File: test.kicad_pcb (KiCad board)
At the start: 2 copper layers, 112 x 43 mm, 41 parts, among them IC1 QFN50P300X300X100-17N-D, IC2 SOT95P280X145-6N, IC3 ESP32-S3-WROOM-1-N16, J1 UART0, J2 73100-0105, J3 73100-0105, K1 AQY210EHA, SW1 Reset, SW2 Boot, U1 USB-C_SMD-TYPE-C-31-M-12, U2 1043, U3 1043, U4 LD1086DT33TR, U5 LD1086DT33TR

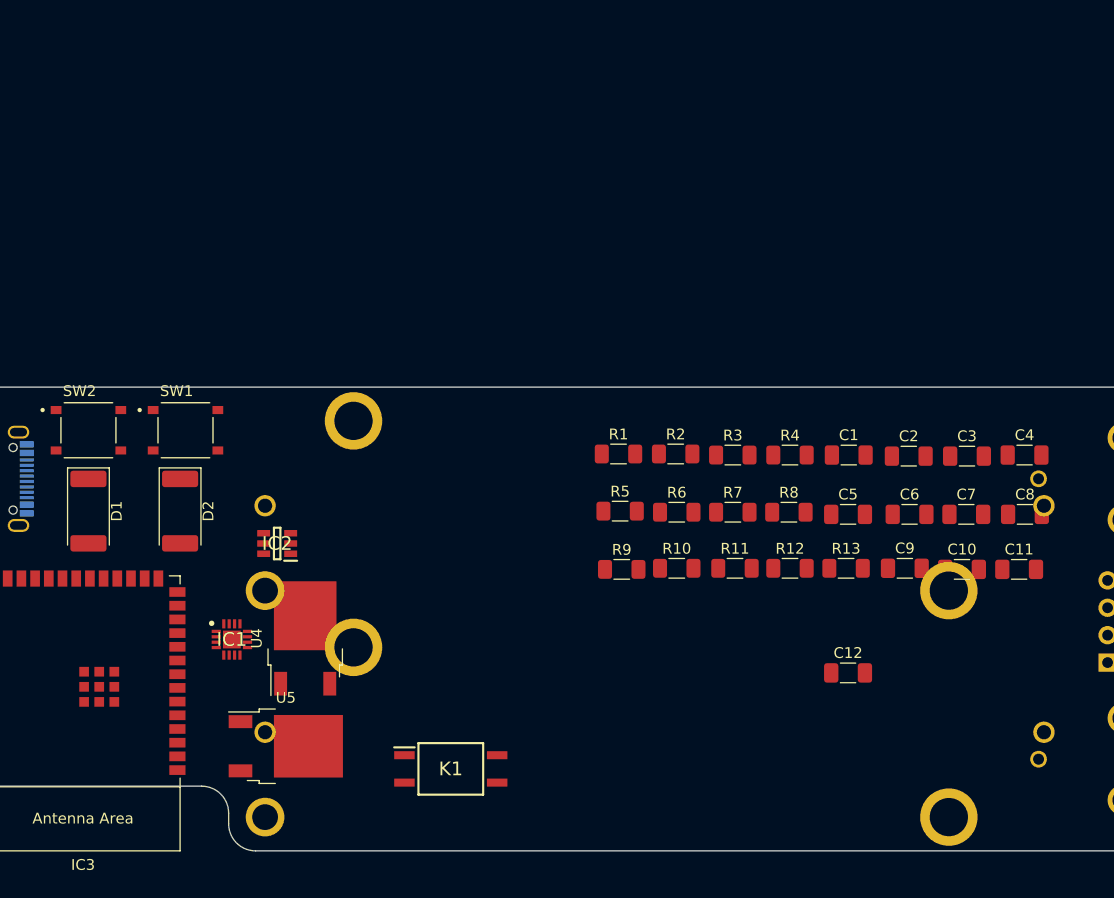
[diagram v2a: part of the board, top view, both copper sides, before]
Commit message: added dac and changed switch, gain
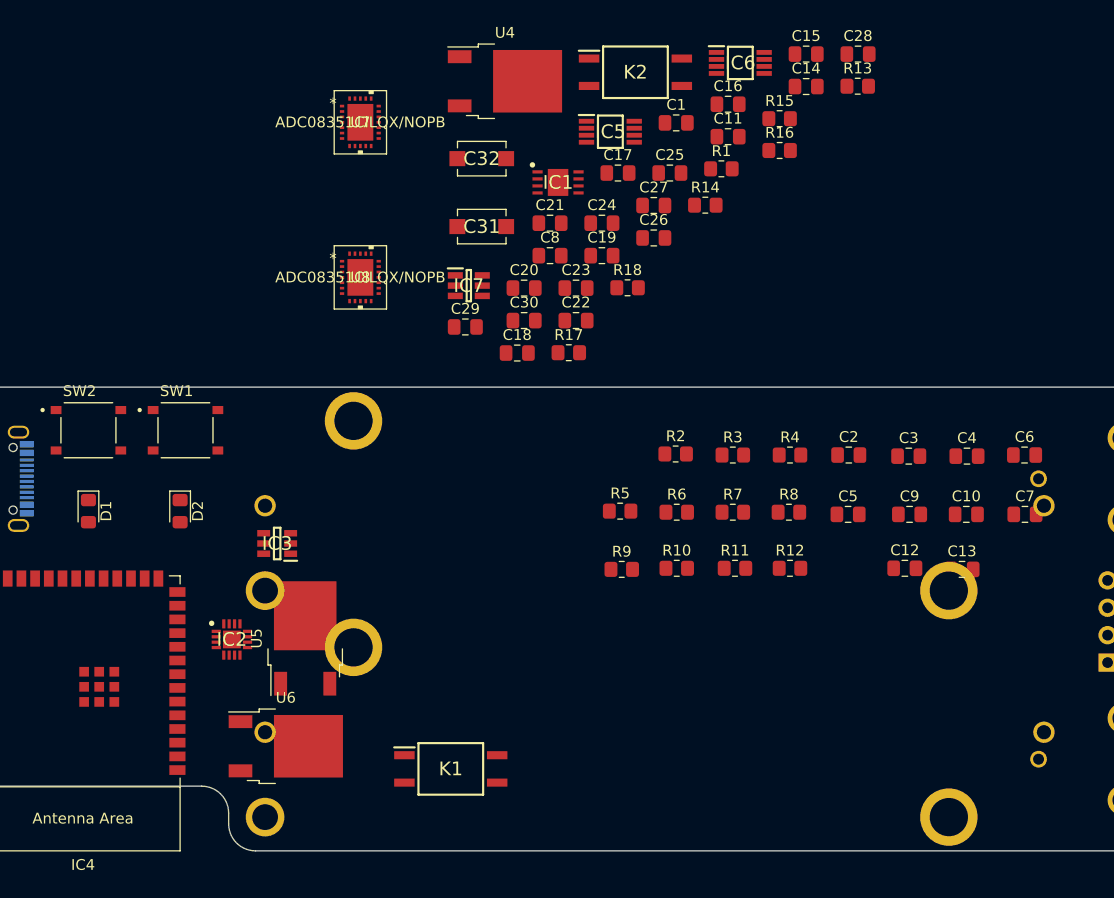
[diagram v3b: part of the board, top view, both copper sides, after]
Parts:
- removed the C12 at (110.9, 116.5)
- added C1: 1u, Capacitor_SMD:C_0805_2012Metric_Pad1.18x1.45mm_HandSolder, F.Cu at (95.0, 65.5)
- added C14: 0.1u, Capacitor_SMD:C_0805_2012Metric_Pad1.18x1.45mm_HandSolder, F.Cu at (107.0, 62.1)
- added C15: 0.1u, Capacitor_SMD:C_0805_2012Metric_Pad1.18x1.45mm_HandSolder, F.Cu at (107.0, 59.1)
- added C16: 0.1u, Capacitor_SMD:C_0805_2012Metric_Pad1.18x1.45mm_HandSolder, F.Cu at (99.8, 63.8)
- added C17: 10u, Capacitor_SMD:C_0805_2012Metric_Pad1.18x1.45mm_HandSolder, F.Cu at (89.6, 70.2)
- added C18: 10u, Capacitor_SMD:C_0805_2012Metric_Pad1.18x1.45mm_HandSolder, F.Cu at (80.3, 86.8)
- added C19: 10u, Capacitor_SMD:C_0805_2012Metric_Pad1.18x1.45mm_HandSolder, F.Cu at (88.1, 77.8)
- added C20: 0.1u, Capacitor_SMD:C_0805_2012Metric_Pad1.18x1.45mm_HandSolder, F.Cu at (80.9, 80.8)
- added C21: 0.1u, Capacitor_SMD:C_0805_2012Metric_Pad1.18x1.45mm_HandSolder, F.Cu at (83.3, 74.8)
- added C22: 0.1u, Capacitor_SMD:C_0805_2012Metric_Pad1.18x1.45mm_HandSolder, F.Cu at (85.7, 83.8)
- added C23: 0.1u, Capacitor_SMD:C_0805_2012Metric_Pad1.18x1.45mm_HandSolder, F.Cu at (85.7, 80.8)
- added C24: 10u, Capacitor_SMD:C_0805_2012Metric_Pad1.18x1.45mm_HandSolder, F.Cu at (88.1, 74.8)
- added C25: 10u, Capacitor_SMD:C_0805_2012Metric_Pad1.18x1.45mm_HandSolder, F.Cu at (94.4, 70.2)
- added C26: 0.1u, Capacitor_SMD:C_0805_2012Metric_Pad1.18x1.45mm_HandSolder, F.Cu at (92.9, 76.2)
- added C27: 47n, Capacitor_SMD:C_0805_2012Metric_Pad1.18x1.45mm_HandSolder, F.Cu at (92.9, 73.2)
- added C28: 47n, Capacitor_SMD:C_0805_2012Metric_Pad1.18x1.45mm_HandSolder, F.Cu at (111.9, 59.1)
- added C29: 100n, Capacitor_SMD:C_0805_2012Metric_Pad1.18x1.45mm_HandSolder, F.Cu at (75.5, 84.4)
- added C30: 100n, Capacitor_SMD:C_0805_2012Metric_Pad1.18x1.45mm_HandSolder, F.Cu at (80.9, 83.8)
- added C31: 5.5p-30p var, project_library:JZ300, F.Cu at (77.0, 75.1)
- added C32: 5.5p-30p var, project_library:JZ300, F.Cu at (77.0, 68.8)
- added C8: 10u, Capacitor_SMD:C_0805_2012Metric_Pad1.18x1.45mm_HandSolder, F.Cu at (83.3, 77.8)
- added IC1: LC709203FQH-01TWG, project_library:LC709203FQH-01TWG, F.Cu at (84.0, 71.0)
- added IC5: MCP6S91-E_MS, project_library:MCP6S91-E_MS, F.Cu at (88.9, 66.3)
- added IC6: MCP6S91-E_MS, project_library:MCP6S91-E_MS, F.Cu at (100.9, 59.9)
- added IC7: MCP4726A1T-E_CH, project_library:MCP4726A1T-E_CH, F.Cu at (75.8, 80.6)
- added K2: AQY210EHA, project_library:AQY210EHAX, F.Cu at (91.2, 60.8)
- added R14: 1k, Resistor_SMD:R_0805_2012Metric_Pad1.20x1.40mm_HandSolder, F.Cu at (97.7, 73.1)
- added R15: 100k, Resistor_SMD:R_0805_2012Metric_Pad1.20x1.40mm_HandSolder, F.Cu at (104.6, 65.1)
- added R16: 100k, Resistor_SMD:R_0805_2012Metric_Pad1.20x1.40mm_HandSolder, F.Cu at (104.6, 68.1)
- added R17: 910k, Resistor_SMD:R_0805_2012Metric_Pad1.20x1.40mm_HandSolder, F.Cu at (85.0, 86.8)
- added R18: 910k, Resistor_SMD:R_0805_2012Metric_Pad1.20x1.40mm_HandSolder, F.Cu at (90.5, 80.8)
- added U4: LD1086DT33TR, Package_TO_SOT_SMD:TO-252-2, F.Cu at (79.1, 61.6)
- added U7: ADC08351CILQX/NOPB, project_library:ADC08351CILQX, F.Cu at (65.7, 65.4)
- added U8: ADC08351CILQX/NOPB, project_library:ADC08351CILQX, F.Cu at (65.7, 79.8)
- C10: renamed from C7; footprint Capacitor_SMD:C_1206_3216Metric_Pad1.33x1.80mm_HandSolder -> Capacitor_SMD:C_0805_2012Metric_Pad1.18x1.45mm_HandSolder
- C11: value 100n -> 10u; footprint Capacitor_SMD:C_1206_3216Metric_Pad1.33x1.80mm_HandSolder -> Capacitor_SMD:C_0805_2012Metric_Pad1.18x1.45mm_HandSolder
- C12: renamed from C9; footprint Capacitor_SMD:C_1206_3216Metric_Pad1.33x1.80mm_HandSolder -> Capacitor_SMD:C_0805_2012Metric_Pad1.18x1.45mm_HandSolder
- C13: renamed from C10; footprint Capacitor_SMD:C_1206_3216Metric_Pad1.33x1.80mm_HandSolder -> Capacitor_SMD:C_0805_2012Metric_Pad1.18x1.45mm_HandSolder
- C2: renamed from C1; footprint Capacitor_SMD:C_1206_3216Metric_Pad1.33x1.80mm_HandSolder -> Capacitor_SMD:C_0805_2012Metric_Pad1.18x1.45mm_HandSolder
- C3: renamed from C2; footprint Capacitor_SMD:C_1206_3216Metric_Pad1.33x1.80mm_HandSolder -> Capacitor_SMD:C_0805_2012Metric_Pad1.18x1.45mm_HandSolder
- C4: renamed from C3; value 100n -> 1u; footprint Capacitor_SMD:C_1206_3216Metric_Pad1.33x1.80mm_HandSolder -> Capacitor_SMD:C_0805_2012Metric_Pad1.18x1.45mm_HandSolder
- C5: footprint Capacitor_SMD:C_1206_3216Metric_Pad1.33x1.80mm_HandSolder -> Capacitor_SMD:C_0805_2012Metric_Pad1.18x1.45mm_HandSolder
- C6: renamed from C4; footprint Capacitor_SMD:C_1206_3216Metric_Pad1.33x1.80mm_HandSolder -> Capacitor_SMD:C_0805_2012Metric_Pad1.18x1.45mm_HandSolder
- C7: renamed from C8; footprint Capacitor_SMD:C_1206_3216Metric_Pad1.33x1.80mm_HandSolder -> Capacitor_SMD:C_0805_2012Metric_Pad1.18x1.45mm_HandSolder
- C9: renamed from C6; footprint Capacitor_SMD:C_1206_3216Metric_Pad1.33x1.80mm_HandSolder -> Capacitor_SMD:C_0805_2012Metric_Pad1.18x1.45mm_HandSolder
- D1: value LED_PowerOn? -> LED_ValidSource; footprint LED_SMD:LED_2512_6332Metric_Pad1.52x3.35mm_HandSolder -> LED_SMD:LED_0805_2012Metric_Pad1.15x1.40mm_HandSolder
- D2: footprint LED_SMD:LED_2512_6332Metric_Pad1.52x3.35mm_HandSolder -> LED_SMD:LED_0805_2012Metric_Pad1.15x1.40mm_HandSolder
- IC2: renamed from IC1; value QFN50P300X300X100-17N-D -> BQ24074RGTR
- IC3: renamed from IC2; value SOT95P280X145-6N -> USBLC6-2SC6
- R1: value 1M -> 10k; footprint Resistor_SMD:R_1206_3216Metric_Pad1.30x1.75mm_HandSolder -> Resistor_SMD:R_0805_2012Metric_Pad1.20x1.40mm_HandSolder
- R10, R11, R12, R2, R3, R4, R5, R6, R7, R8, R9: footprint Resistor_SMD:R_1206_3216Metric_Pad1.30x1.75mm_HandSolder -> Resistor_SMD:R_0805_2012Metric_Pad1.20x1.40mm_HandSolder
- R13: value 5k1 -> 1k; footprint Resistor_SMD:R_1206_3216Metric_Pad1.30x1.75mm_HandSolder -> Resistor_SMD:R_0805_2012Metric_Pad1.20x1.40mm_HandSolder
- moved C11 48.4 mm to (99.8, 66.8)
- moved R13 44.7 mm to (111.8, 62.1)
- moved R1 28.1 mm to (99.2, 69.8)
- renumbered IC3 to IC4, J3 to J2, J2 to J3, U2 to U1, U3 to U2, U4 to U5, U5 to U6
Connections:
- net Net-(C3-Pad1) renamed /ENABLE
- net Net-(D1-Pad1) renamed /ValidUSB
- C11 pad 1: Net-(C11-Pad1) -> +3V3
- C12 pad 1: +3V3 -> +3.3VA
- D2 pad 1: Net-(D2-Pad1) -> /Charging
- IC2 pad 1: unconnected-(IC1-Pad1) -> Net-(IC2-Pad1)
- IC2 pad 15: GND -> +5V
- IC2 pad 9: Net-(D2-Pad1) -> /Charging
- IC3 pad 4: Net-(IC2-Pad4) -> Net-(IC3-Pad4)
- IC3 pad 6: Net-(IC2-Pad6) -> Net-(IC3-Pad6)
- IC4 pad 10: unconnected-(IC3-Pad10) -> /CH1_D6
- IC4 pad 11: unconnected-(IC3-Pad11) -> /CH1_D7
- IC4 pad 12: unconnected-(IC3-Pad12) -> /I2S_CLK
- IC4 pad 15: unconnected-(IC3-Pad15) -> /CH2_D0
- IC4 pad 16: unconnected-(IC3-Pad16) -> /LOG
- IC4 pad 17: unconnected-(IC3-Pad17) -> /CH2_D1
- IC4 pad 18: unconnected-(IC3-Pad18) -> /CH2_D2
- IC4 pad 19: unconnected-(IC3-Pad19) -> /MOSI
- IC4 pad 20: /MISO -> /SCLK
- IC4 pad 21: /MOSI -> /CH2_D3
- IC4 pad 22: /SCLK -> /CH2_D4
- IC4 pad 23: unconnected-(IC3-Pad23) -> /CH2_D5
- IC4 pad 24: unconnected-(IC3-Pad24) -> /CH2_D6
- IC4 pad 25: unconnected-(IC3-Pad25) -> /CH2_D7
- IC4 pad 26: unconnected-(IC3-Pad26) -> /VSPI
- IC4 pad 27: Net-(C11-Pad1) -> /BOOT
- IC4 pad 31: unconnected-(IC3-Pad31) -> /CH1_Gnd_Sel
- IC4 pad 32: unconnected-(IC3-Pad32) -> /CH2_Gnd_Sel
- IC4 pad 33: unconnected-(IC3-Pad33) -> /CS_A
- IC4 pad 34: unconnected-(IC3-Pad34) -> /CS_B
- IC4 pad 35: unconnected-(IC3-Pad35) -> /Charging
- IC4 pad 38: unconnected-(IC3-Pad38) -> /SCL
- IC4 pad 39: unconnected-(IC3-Pad39) -> /SDA
- IC4 pad 4: unconnected-(IC3-Pad4) -> /CH1_D0
- IC4 pad 5: unconnected-(IC3-Pad5) -> /CH1_D1
- IC4 pad 6: unconnected-(IC3-Pad6) -> /CH1_D2
- IC4 pad 7: unconnected-(IC3-Pad7) -> /CH1_D3
- IC4 pad 8: /CS -> /CH1_D4
- IC4 pad 9: unconnected-(IC3-Pad9) -> /CH1_D5
- J2 pad 1: unconnected-(J3-Pad1) -> /PGND
- J2 pad 2: unconnected-(J3-Pad2) -> /PGND
- J2 pad 3: unconnected-(J3-Pad3) -> Net-(C31-Pad1)
- J3 pad 1: unconnected-(J2-Pad1) -> /PGND
- J3 pad 2: unconnected-(J2-Pad2) -> /PGND
- J3 pad 3: unconnected-(J2-Pad3) -> Net-(C32-Pad1)
- K1 pad 1: unconnected-(K1-Pad1) -> /CH1_Gnd_Sel
- K1 pad 2: unconnected-(K1-Pad2) -> Net-(K1-Pad2)
- K1 pad 3: unconnected-(K1-Pad3) -> Net-(C29-Pad1)
- K1 pad 4: unconnected-(K1-Pad4) -> Net-(C27-Pad1)
- R1 pad 1: Net-(R1-Pad1) -> GND
- R1 pad 2: GND -> Net-(IC2-Pad1)
- R13 pad 1: +3V3 -> GND
- R13 pad 2: Net-(C11-Pad1) -> Net-(K1-Pad2)
- U5 pad 2: +3V3 -> +3.3VA

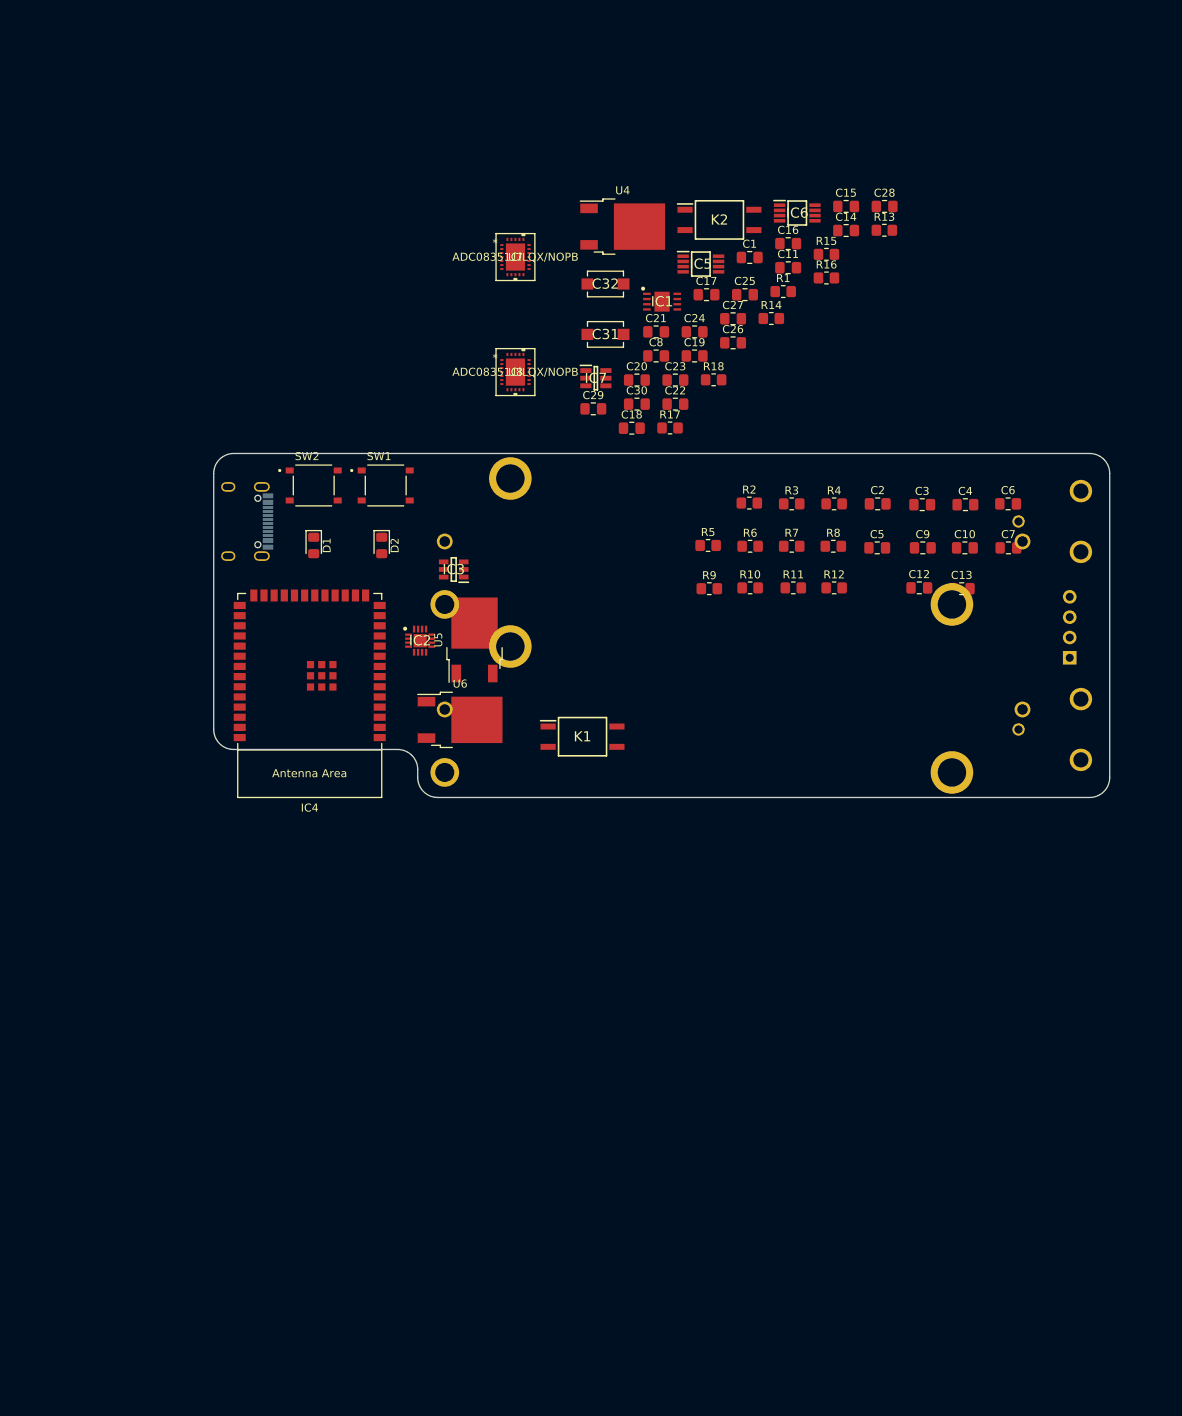
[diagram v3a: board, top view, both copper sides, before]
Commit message: grouped footprints
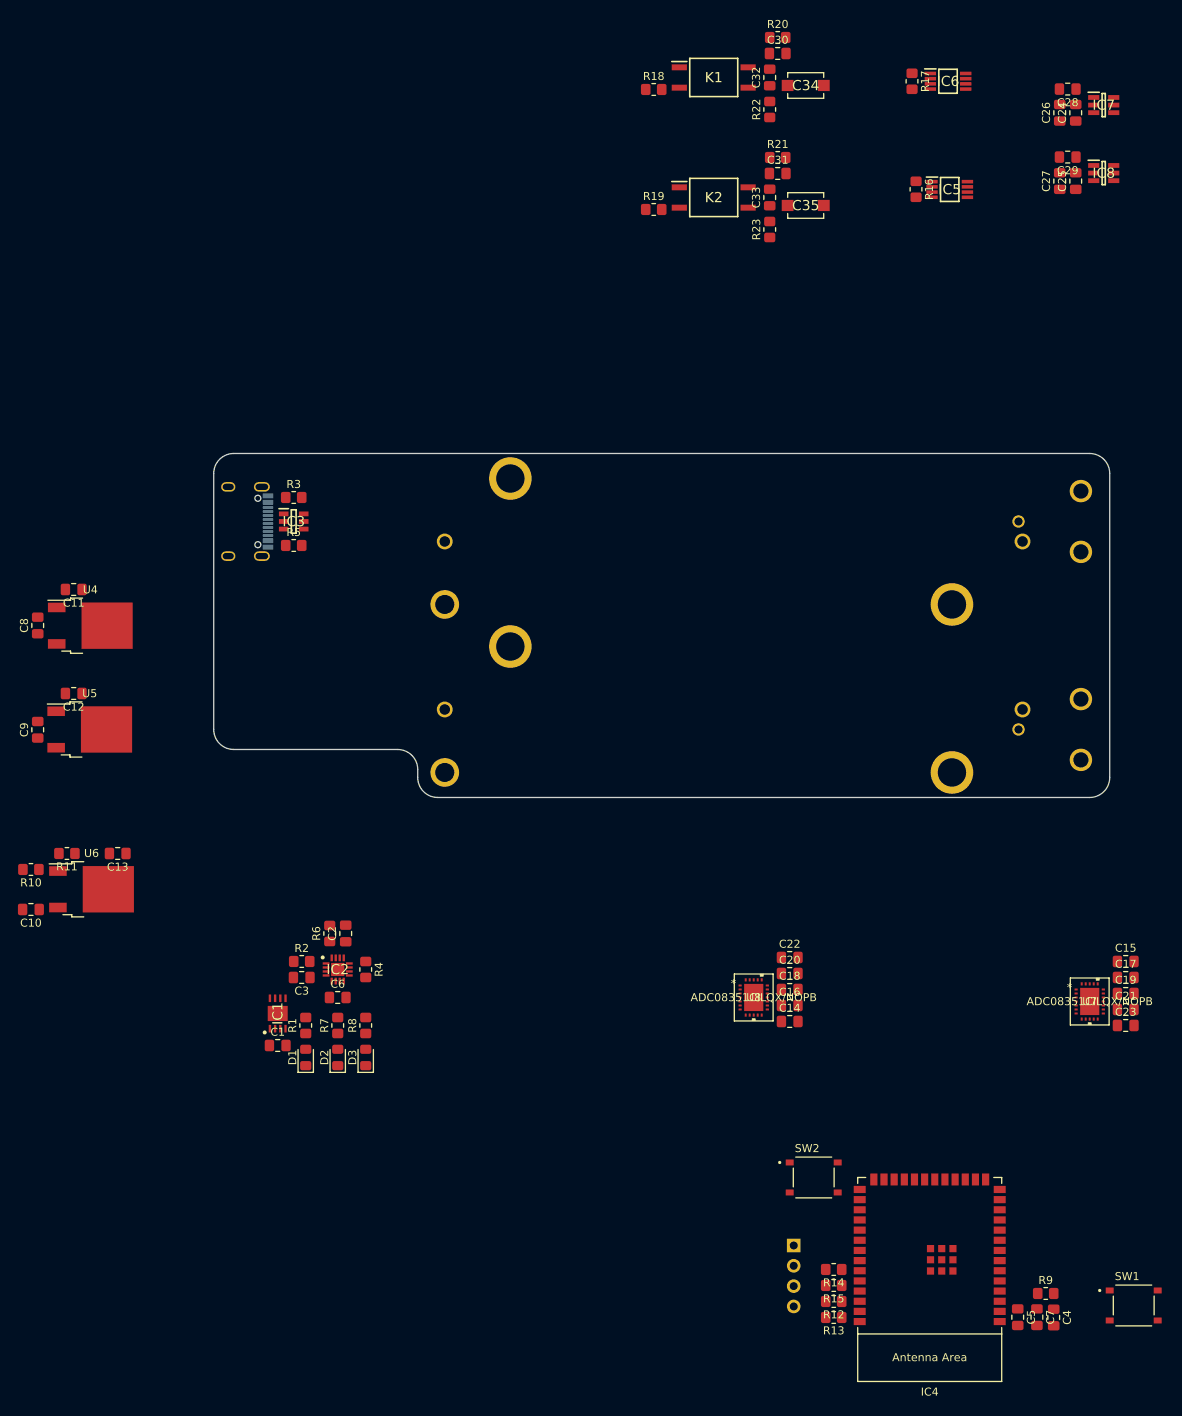
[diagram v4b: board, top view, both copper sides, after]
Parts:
- added C25: 0.1u, Capacitor_SMD:C_0805_2012Metric_Pad1.18x1.45mm_HandSolder, F.Cu at (135.8, 56.0)
- added C27: 10u, Capacitor_SMD:C_0805_2012Metric_Pad1.18x1.45mm_HandSolder, F.Cu at (133.8, 56.0)
- added C29: 0.1u, Capacitor_SMD:C_0805_2012Metric_Pad1.18x1.45mm_HandSolder, F.Cu at (134.8, 53.0)
- added D1: LOW_BATTERY, LED_SMD:LED_0805_2012Metric_Pad1.15x1.40mm_HandSolder, F.Cu at (39.5, 165.5)
- added IC8: SOT95P270X145-6N, project_library:MCP4726A1T-E_CH, F.Cu at (139.2, 55.0)
- added R1: 1k5, Resistor_SMD:R_0805_2012Metric_Pad1.20x1.40mm_HandSolder, F.Cu at (39.5, 161.5)
- added R12: 5k, Resistor_SMD:R_0805_2012Metric_Pad1.20x1.40mm_HandSolder, F.Cu at (105.5, 196.0)
- added R13: 5k, Resistor_SMD:R_0805_2012Metric_Pad1.20x1.40mm_HandSolder, F.Cu at (105.5, 198.0)
- added R16: 5k1, Resistor_SMD:R_0805_2012Metric_Pad1.20x1.40mm_HandSolder, F.Cu at (115.8, 57.0)
- added R17: 5k1, Resistor_SMD:R_0805_2012Metric_Pad1.20x1.40mm_HandSolder, F.Cu at (115.3, 43.5)
- IC1: value LC709203FQH-01TWG -> SON65P400X300X80-9N
- IC2: value BQ24074RGTR -> QFN50P300X300X100-17N-D
- IC3: value USBLC6-2SC6 -> SOT95P280X145-6N
- IC5, IC6: value MCP6S91-E_MS -> SOP65P488X118-8N
- IC7: value MCP4726A1T-E_CH -> SOT95P270X145-6N
- moved SW1 138.7 mm to (143.0, 196.5)
- moved C10 125.2 mm to (5.15, 147.0), turned to 180 degrees
- moved U7 117.5 mm to (137.5, 158.5)
- moved C1 114.8 mm to (36.0, 164.0)
- moved C9 112.9 mm to (6.00, 124.5), turned to 90 degrees
- moved C13 110.6 mm to (16.0, 140.0), turned to 180 degrees
- moved SW2 106.7 mm to (103.0, 180.5)
- moved C12 106.5 mm to (10.5, 120.0), turned to 180 degrees
- moved IC4 106.5 mm to (117.5, 190.2)
- moved C6 104.1 mm to (43.5, 158.0)
- moved R2 103.1 mm to (39.0, 153.5)
- moved C23 103.0 mm to (142.0, 161.5)
- moved C4 102.2 mm to (133.0, 198.0), turned to -90 degrees
- moved C19 101.4 mm to (142.0, 157.5)
- moved IC1 101.1 mm to (36.0, 160.0), turned to 90 degrees
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- renumbered C17 to C16, C18 to C17, C20 to C18, C21 to C19, C22 to C20, C23 to C21, C24 to C22, C25 to C23, C16 to C24, C19 to C26, C26 to C28, C27 to C30, C28 to C31, C29 to C32, C30 to C33, C31 to C34, C32 to C35, D1 to D2, D2 to D3, R9 to R10, R10 to R11, R11 to R14, R12 to R15, R13 to R18, R14 to R19, R1 to R2, R15 to R20, R16 to R21, R17 to R22, R18 to R23, R2 to R3, R3 to R4, R4 to R5, R5 to R6, R6 to R7, R7 to R8, R8 to R9
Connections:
- C13 pad 1: /PGND -> GND
- IC5 pad 1: unconnected-(IC5-Pad1) -> Net-(IC5-Pad1)
- IC5 pad 3: unconnected-(IC5-Pad3) -> GND
- IC5 pad 4: unconnected-(IC5-Pad4) -> GND
- IC5 pad 5: unconnected-(IC5-Pad5) -> /CS_A
- IC5 pad 6: unconnected-(IC5-Pad6) -> /MOSI
- IC5 pad 7: unconnected-(IC5-Pad7) -> /SCLK
- IC5 pad 8: unconnected-(IC5-Pad8) -> +3V3
- IC6 pad 1: unconnected-(IC6-Pad1) -> Net-(IC6-Pad1)
- IC6 pad 3: unconnected-(IC6-Pad3) -> GND
- IC6 pad 4: unconnected-(IC6-Pad4) -> GND
- IC6 pad 5: unconnected-(IC6-Pad5) -> /CS_A
- IC6 pad 6: unconnected-(IC6-Pad6) -> /MOSI
- IC6 pad 7: unconnected-(IC6-Pad7) -> /SCLK
- IC6 pad 8: unconnected-(IC6-Pad8) -> +3V3
- J1 pad 2: /RX0 -> /RX
- J1 pad 3: /TX0 -> /TX
- R11 pad 1: /PGND -> GND
- R14 pad 2: /RX0 -> /RX
- R15 pad 2: /TX0 -> /TX
- R3 pad 1: Net-(R2-Pad1) -> Net-(R3-Pad1)
- R5 pad 1: Net-(R4-Pad1) -> Net-(R5-Pad1)
- U6 pad 2: /PGND -> GND
